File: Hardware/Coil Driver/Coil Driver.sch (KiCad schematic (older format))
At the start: 57 parts

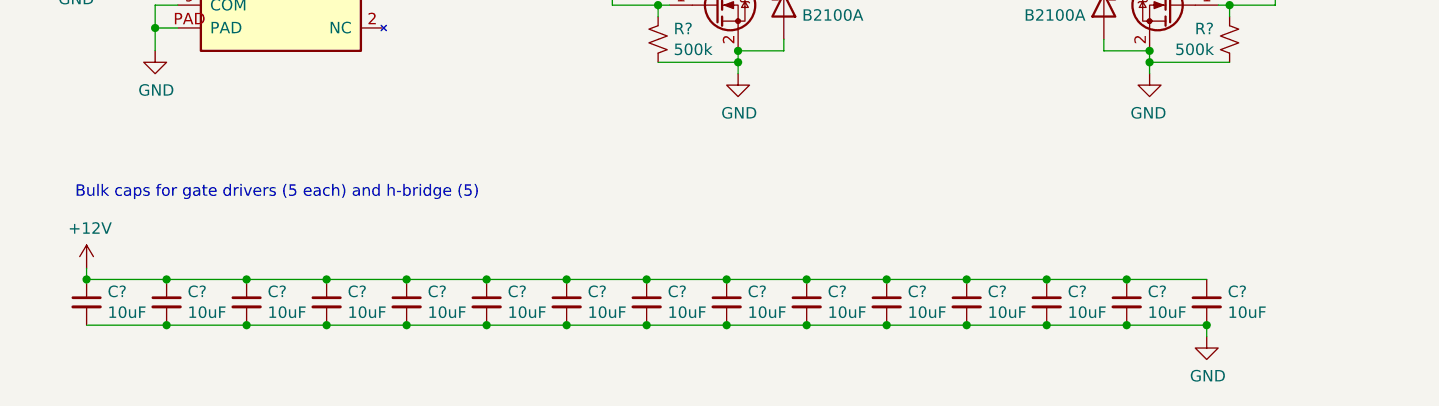
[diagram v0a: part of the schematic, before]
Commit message: moving .gitignore to hardware folder to prepare for committing firmware folder. Also modified decoupling caps for gate drivers
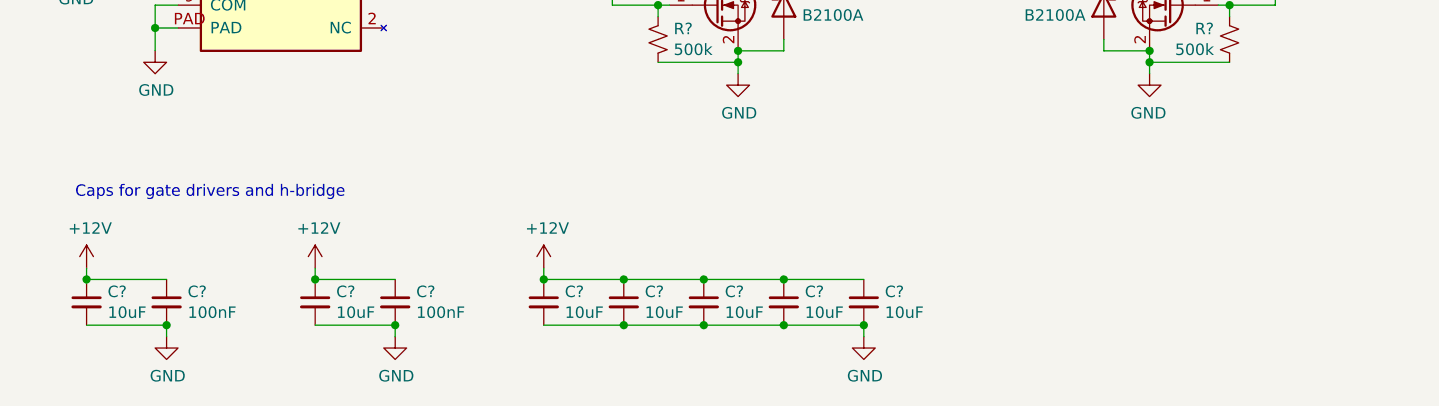
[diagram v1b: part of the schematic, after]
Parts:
- removed C? (x9): 10uF, symbol Device:C_Small
- added C? (x2): 100nF, symbol Device:C_Small
- added C?: 10uF, symbol Device:C_Small
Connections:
- net +12V: now also C?.1, C?.1, C?.1
- net GND: now also C?.2, C?.2, C?.2
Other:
- note added: "Caps for gate drivers and h-bridge"
- note removed: "Bulk caps for gate drivers (5 each) and h-bridge (5)"
- moved on the sheet: C?

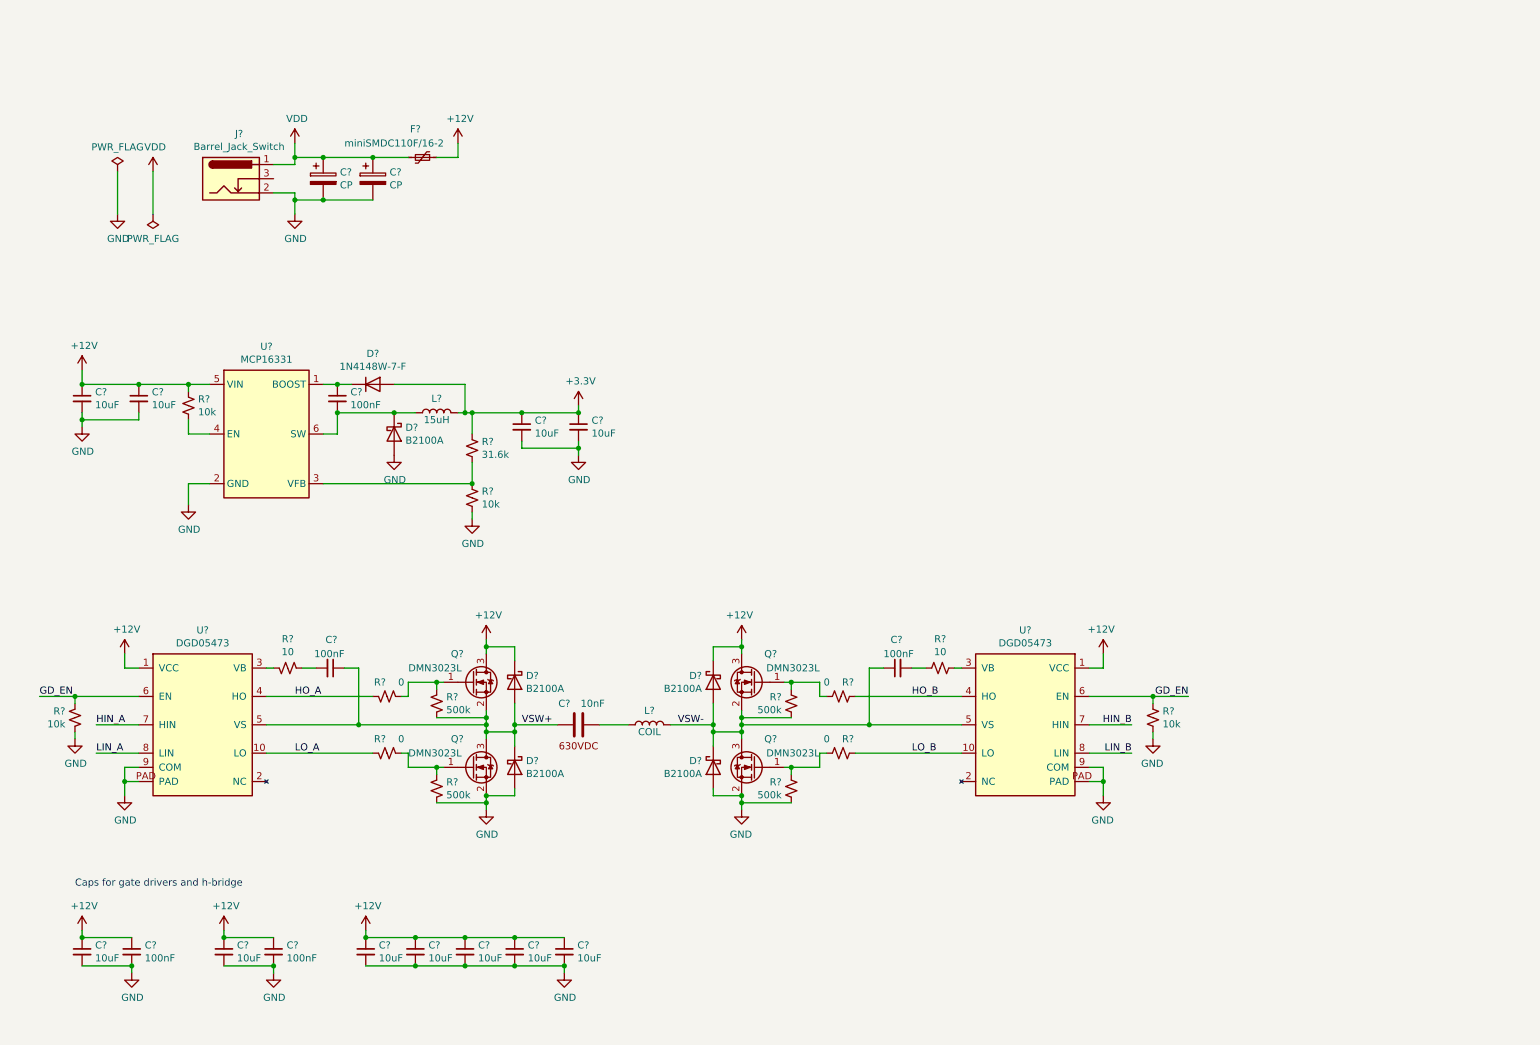
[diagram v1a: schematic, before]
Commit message: added micro and button to library, added microcontroller to schematic, added boxes and title block info, and annotated refdes
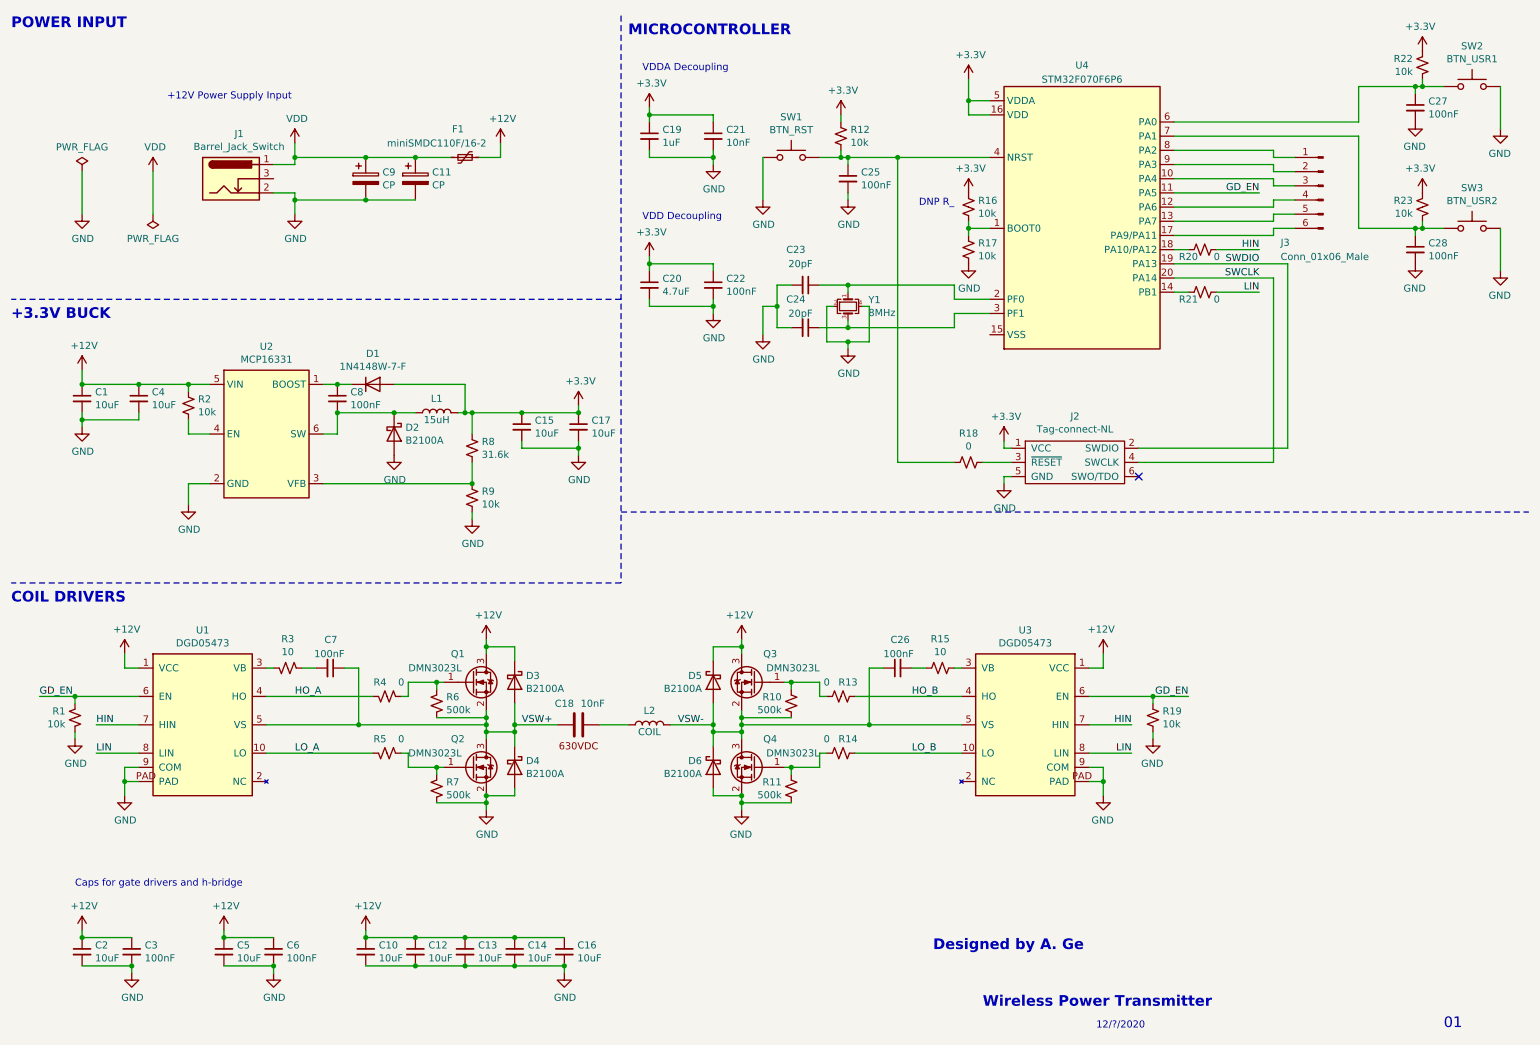
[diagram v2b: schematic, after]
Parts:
- added C19: 1uF, symbol Device:C_Small
- added C20: 4.7uF, symbol Device:C_Small
- added C21: 10nF, symbol Device:C_Small
- added C22, C25, C27, C28: 100nF, symbol Device:C_Small
- added C23, C24: 20pF, symbol Device:C_Small
- added J2: Tag-connect-NL, symbol Tag-connect:Tag-connect-NL
- added J3: Conn_01x06_Male, symbol Connector:Conn_01x06_Male
- added R12, R16, R17, R22, R23: 10k, symbol Device:R_Small_US
- added R18, R20, R21: 0, symbol Device:R_Small_US
- added SW1: BTN_RST, MyParts:PTS647, symbol MyParts:PTS647
- added SW2: BTN_USR1, MyParts:PTS647, symbol MyParts:PTS647
- added SW3: BTN_USR2, MyParts:PTS647, symbol MyParts:PTS647
- added U4: STM32F070F6P6, Package_SO:TSSOP-20_4.4x6.5mm_P0.65mm, symbol MyParts:STM32F070F6P6
- added Y1: 8MHz, symbol Device:Crystal_GND24_Small
- gave numbers to parts that had none: 51
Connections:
- net HIN_B is gone; now on net HIN: U3.7 (HIN)
- net LIN_B is gone; now on net LIN: U3.8 (LIN)
- net +3V3: now also C19.1, C20.1, C21.1, C22.1, J2.1 (VCC), R12.1, R16.1, R22.1, R23.1, U4.16 (VDD), U4.5 (VDDA)
- net GD_EN: now also U4.11 (PA5)
- net GND: now also C19.2, C20.2, C21.2, C22.2, C23.2, C24.2, C25.2, C27.2, C28.2, J2.5 (GND), R17.2, SW1.1, SW2.1, SW3.1, Y1.2, Y1.4
- net HIN_A renamed HIN
- net HIN: now also R20.1
- net LIN_A renamed LIN
- net LIN: now also R21.1
- new net: R16.2, R17.1, U4.1 (BOOT0)
- new net: J3.3 (Pin_3), U4.10 (PA4)
- new net: J3.4 (Pin_4), U4.12 (PA6)
- new net: J3.5 (Pin_5), U4.13 (PA7)
- new net: R21.2, U4.14 (PB1)
- new net: J3.6 (Pin_6), U4.17 (PA9/PA11)
- new net: R20.2, U4.18 (PA10/PA12)
- new net: C23.1, U4.2 (PF0), Y1.1
- new net: C24.1, U4.3 (PF1), Y1.3
- new net: C25.1, R12.2, R18.2, SW1.2, U4.4 (NRST)
- new net: C27.1, R22.2, SW2.2, U4.6 (PA0)
- new net: C28.1, R23.2, SW3.2, U4.7 (PA1)
- new net: J3.1 (Pin_1), U4.8 (PA2)
- new net: J3.2 (Pin_2), U4.9 (PA3)
- new net: J2.3 (~RESET), R18.1
- new net SWCLK: J2.4 (SWCLK), U4.20 (PA14)
- new net SWDIO: J2.2 (SWDIO), U4.19 (PA13)
- no-connect marks 0 -> 1
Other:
- note added: "+12V Power Supply Input"
- note added: "+3.3V BUCK"
- note added: "01"
- note added: "12/?/2020"
- note added: "COIL DRIVERS"
- note added: "DNP R_"
- note added: "Designed by A. Ge"
- note added: "MICROCONTROLLER"
- note added: "POWER INPUT"
- note added: "VDD Decoupling"
- note added: "VDDA Decoupling"
- note added: "Wireless Power Transmitter"
- moved on the sheet: C11, C9, F1

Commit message: Added power flags, passing ERC
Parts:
- added J2: Conn_01x02_Male, symbol Connector:Conn_01x02_Male
- renumbered C12 to C10, C9 to C11, C13 to C12, C11 to C13, C10 to C9, J2 to J3, J3 to J4
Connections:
- net GND: now also U4.15 (VSS), J2.2 (Pin_2)
- net VDD: now also J2.1 (Pin_1)
- no-connect marks 1 -> 2
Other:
- moved on the sheet: C11, C13, F1

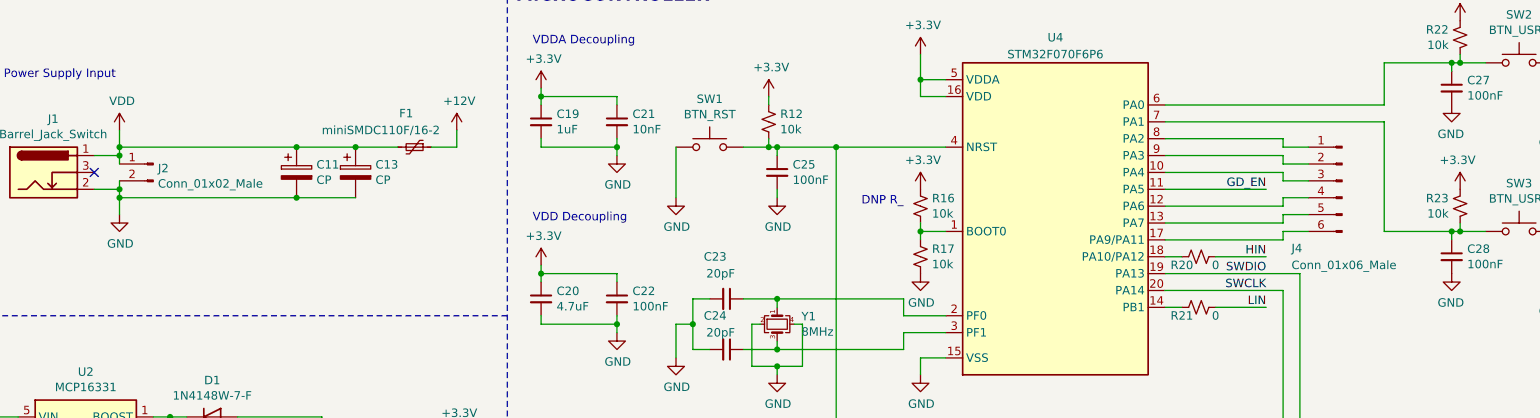
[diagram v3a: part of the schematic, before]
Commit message: added footprint for resettable fuse
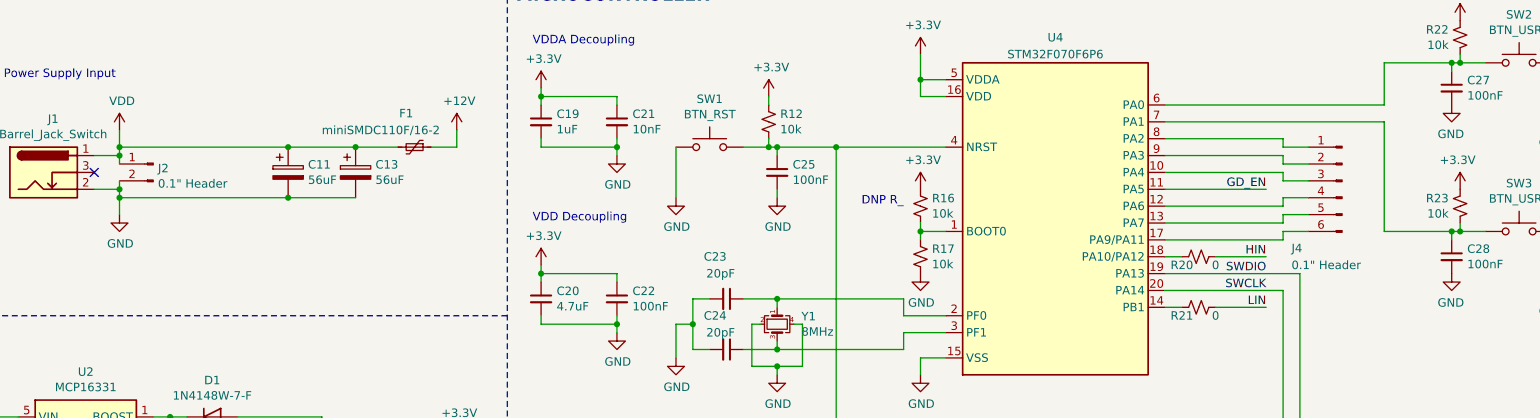
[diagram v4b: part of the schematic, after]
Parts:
- C1, C10, C12, C14, C15, C16, C17, C19, C2, C20, C4, C5, C6, C7, C8, C9: footprint (none) -> Capacitor_SMD:C_0603_1608Metric
- C11, C13: value CP -> 56uF; footprint (none) -> Capacitor_SMD:CP_Elec_6.3x7.7
- C21, C22, C23, C24, C25, C26, C27, C28, C3: footprint (none) -> Capacitor_SMD:C_0402_1005Metric
- F1: footprint (none) -> MyParts:miniSMDC110F_16-2
- J1: footprint (none) -> Connector_BarrelJack:BarrelJack_CUI_PJ-102AH_Horizontal
- J2: value Conn_01x02_Male -> 0.1\" Header; footprint (none) -> Connector_PinHeader_2.54mm:PinHeader_1x02_P2.54mm_Vertical
- J3: footprint (none) -> Tag-connect:TC2030-IDC-NL-FP
- J4: value Conn_01x06_Male -> 0.1\" Header; footprint (none) -> Connector_PinHeader_2.54mm:PinHeader_1x06_P2.54mm_Vertical
- L2: footprint (none) -> Connector_PinHeader_2.54mm:PinHeader_1x02_P2.54mm_Vertical
- R1, R10, R11, R12, R13, R14, R15, R16, R17, R18, R19, R2, R20, R21, R22, R23, R3, R4, R5, R6, R7, R8, R9: footprint (none) -> Resistor_SMD:R_0603_1608Metric
- Y1: footprint (none) -> Crystal:Crystal_SMD_5032-4Pin_5.0x3.2mm
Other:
- moved on the sheet: C11

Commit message: changed WIMA cap to be standard capacitor part with new parameters
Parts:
- removed C18: 10nF, Capacitor_THT:C_Rect_L7.2mm_W4.5mm_P5.00mm_FKS2_FKP2_MKS2_MKP2, symbol MyParts:10nF
- added C18: 10nF, Capacitor_THT:C_Rect_L7.2mm_W8.5mm_P5.00mm_FKS2_FKP2_MKS2_MKP2, symbol Device:C
- L1: footprint (none) -> Inductor_SMD:L_Wuerth_HCI-5040
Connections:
- net VSW+: now also C18.2
- net at L2.1: now also C18.1
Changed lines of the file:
@@
 	4050 5350 4050 5500
-$Comp
-L MyParts:10nF C18
-U 1 1 5FBAD0E5
-P 4500 5500
-F 0 "C18" V 4350 5400 50  0000 C CNN
-F 1 "10nF" V 4350 5600 50  0000 C CNN
-F 2 "Capacitor_THT:C_Rect_L7.2mm_W4.5mm_P5.00mm_FKS2_FKP2_MKS2_MKP2" H 4538 5350 50  0001 C CNN
-F 3 "https://www.wima.de/wp-content/uploads/media/e_WIMA_MKP_2.pdf" H 4500 5500 50  0001 C CNN
-	1    4500 5500
-	0    1    1    0
-$EndComp
 $Comp
 L Device:L L2
@@
 F 0 "L1" V 3600 3300 50  0000 C CNN
 F 1 "15uH" V 3450 3300 50  0000 C CNN
-F 2 "" H 3500 3300 50  0001 C CNN
+F 2 "Inductor_SMD:L_Wuerth_HCI-5040" H 3500 3300 50  0001 C CNN
 F 3 "~" H 3500 3300 50  0001 C CNN
 	1    3500 3300
@@
 	1    0    0    -1
 $EndComp
+$Comp
+L Device:C C18
+U 1 1 5FE6940C
+P 4500 5500
+F 0 "C18" V 4350 5400 50  0000 C CNN
+F 1 "10nF" V 4350 5600 50  0000 C CNN
+F 2 "Capacitor_THT:C_Rect_L7.2mm_W8.5mm_P5.00mm_FKS2_FKP2_MKS2_MKP2" H 4538 5350 50  0001 C CNN
+F 3 "https://www.wima.de/wp-content/uploads/media/e_WIMA_MKP_2.pdf" H 4500 5500 50  0001 C CNN
+F 4 "630VDC" V 4650 5500 50  0000 C CNN "Voltage Rating"
+F 5 "FKP2J021001L00JSC9" V 4500 5500 50  0001 C CNN "MPN"
+	1    4500 5500
+	0    1    1    0
+$EndComp
 $EndSCHEMATC

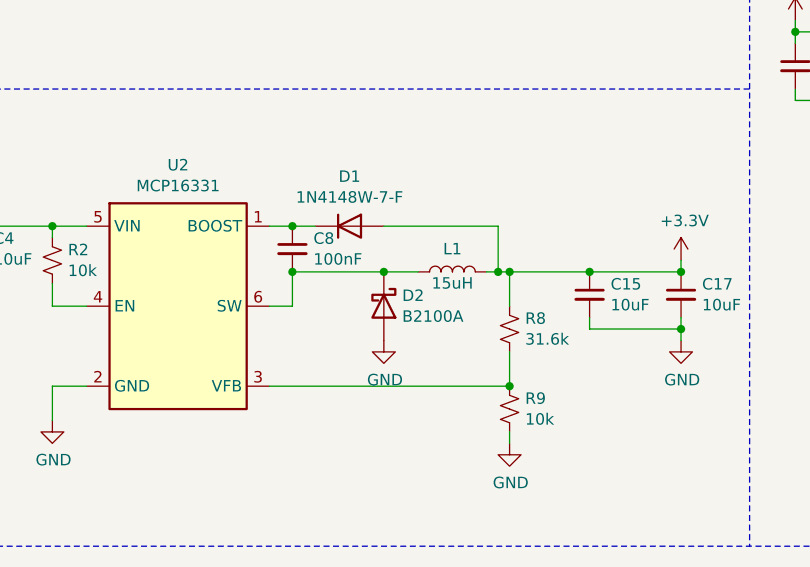
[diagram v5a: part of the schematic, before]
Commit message: created footprint for inductor and added parameters to schematic. Added switch footprint. Added several missing STEP models. Note that updating all from library may reset paths and cause STEPs from KiCad default components to disappear again.
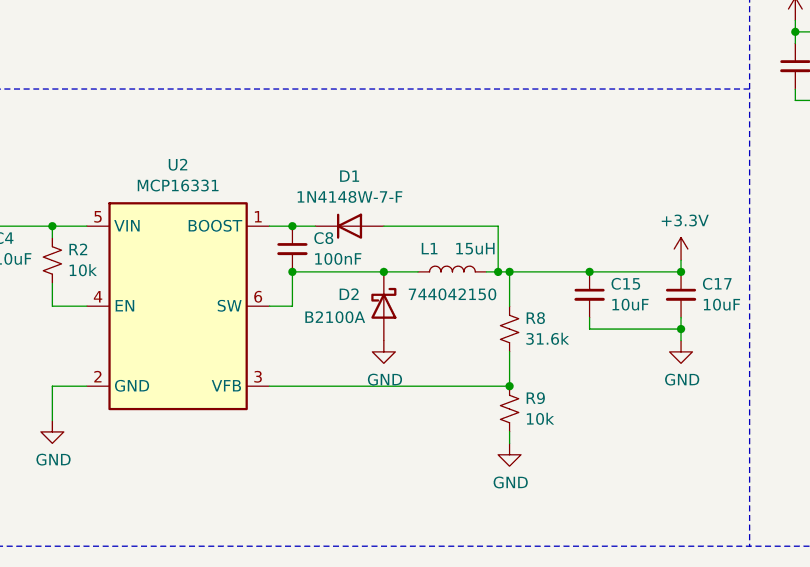
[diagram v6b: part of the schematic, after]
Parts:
- L1: footprint Inductor_SMD:L_Wuerth_HCI-5040 -> MyParts:744042150; Ir (none) -> 1.03A; Isat (none) -> 0.75A; MPN (none) -> 744042150
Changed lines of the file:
@@
 U 1 1 5FB83E83
 P 3200 3450
-F 0 "D2" V 3154 3530 50  0000 L CNN
-F 1 "B2100A" V 3245 3530 50  0000 L CNN
+F 0 "D2" V 3150 3250 50  0000 L CNN
+F 1 "B2100A" V 3250 3100 50  0000 L CNN
 F 2 "Diode_SMD:D_SMA" H 3200 3275 50  0001 C CNN
 F 3 "https://www.diodes.com/assets/Datasheets/B2100A.pdf" H 3200 3450 50  0001 C CNN
@@
 U 1 1 5FB82AFC
 P 3500 3300
-F 0 "L1" V 3600 3300 50  0000 C CNN
-F 1 "15uH" V 3450 3300 50  0000 C CNN
-F 2 "Inductor_SMD:L_Wuerth_HCI-5040" H 3500 3300 50  0001 C CNN
-F 3 "~" H 3500 3300 50  0001 C CNN
+F 0 "L1" V 3600 3400 50  0000 C CNN
+F 1 "15uH" V 3600 3200 50  0000 C CNN
+F 2 "MyParts:744042150" H 3500 3300 50  0001 C CNN
+F 3 "https://www.we-online.de/katalog/datasheet/744042150.pdf" H 3500 3300 50  0001 C CNN
+F 4 "744042150" V 3400 3300 50  0000 C CNN "MPN"
+F 5 "0.75A" V 3500 3300 50  0001 C CNN "Isat"
+F 6 "1.03A" V 3500 3300 50  0001 C CNN "Ir"
 	1    3500 3300
 	0    -1   -1   0
